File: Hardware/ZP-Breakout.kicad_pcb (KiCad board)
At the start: 4 copper layers, 100 x 75 mm, 196 parts, among them J1 GH-6, J10 GH-4, J11 GH-3, J12 GH-4, J13 GH-2, J14 GH-4, J15 GH-4, J16 GH-4, J17 GH-4, J18 GH-6, J19 GH-6, J2 GH-6, J20 GH-6, J21 GH-6, J22 GH-6, J23 GH-6, J24 GH-2, J25 GH-4, J26 GH-4, J27 GH-4, J28 GH-4, J29 GH-6, J3 GH-6, J30 Conn_02x02_Odd_Even, J31 Conn_01x02, J4 GH-6, J5 GH-6, J6 GH-6, J7 GH-2, J8 Micro_SD_Card, J9 USB_MICRO_B, Q1 BSS84LT1G, Q2 BSS138, Q3 BSS84LT1G, SW1 SW_Push_Dual_1-2short_3-4short, SW2 SW_Push_Dual_1-2short_3-4short, U1 MCP1826S-3302E/DB, U4 STM32F765ZGT6, U5 M24C64-WDW6TP, U6 ICM-20602, U7 MS5637-02BA03, U8 FT4232H, U9 STM32F091RCT7, Y1 32.768kHz, Y2 8MHz, Y3 Crystal_GND24, Y4 32.768kHz, Y5 8MHz

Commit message: Finished routing. TODO: Silk.
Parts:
- J27: value GH-4 -> GH-2; footprint Connector_PinHeader_2.54mm:PinHeader_1x04_P2.54mm_Vertical -> Connector_PinHeader_2.54mm:PinHeader_1x02_P2.54mm_Vertical
- moved J29 64.7 mm to (113.3, 93.5)
- moved J27 55.6 mm to (102.2, 98.3), turned to 270 degrees
- moved J23 32.4 mm to (104.4, 138.2)
- moved R8 20.3 mm to (59.1, 136.6)
- moved R9 20.2 mm to (60.7, 136.6), turned to 270 degrees
- moved D16 20.1 mm to (62.4, 136.7)
- moved J15 18.4 mm to (78.7, 143.2)
- moved J16 18.4 mm to (78.7, 138.2)
- moved D15 15.9 mm to (62.4, 139.9), turned to 90 degrees
- moved R7 15.1 mm to (60.7, 140.1)
- moved D2 14.7 mm to (81.2, 98.8), turned to 180 degrees
- moved Q1 13.7 mm to (84.3, 96.1), turned to 270 degrees
- moved J28 13.7 mm to (97.0, 153.1)
- moved J19 13.6 mm to (104.4, 143.1)
- moved J12 12.8 mm to (109.8, 153.2)
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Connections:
- J27 pad 1: GND -> /SCL1
- J27 pad 2: /SCL1 -> /SDA1
- J30 pad 2: /5V_INT -> /6V_EXT
- J30 pad 4: /6V_EXT -> /5V_INT
- Q1 pad 2: /5V_INT -> /3V3
- Q3 pad 2: /5V_INT -> /3V3
- R1 pad 2: /5V_INT -> /3V3
- R2 pad 2: /5V_INT -> /3V3
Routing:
- net /3V3: track 198.5 -> 248.4 mm, vias 30 -> 41
- net /NRST_SAFETY: track 31.5 -> 80.6 mm
- net /5V_INT: track 25.2 -> 72.3 mm, vias 2 -> 24
- net /NRST_PILOT: track 47.7 -> 88.1 mm, vias 7 -> 8
- net /NSS5: track 0.00 -> 36.3 mm, vias 0 -> 1
- net /AIRSPD_ADC: track 36.7 -> 72.7 mm
- net /ULTRA_SONIC_2: track 38.5 -> 73.8 mm, vias 1 -> 2
- net /CTS1: track 38.6 -> 72.1 mm, vias 4 -> 3
- net /TX2: track 6.13 -> 37.9 mm, vias 0 -> 1
- net /SDA4: track 7.46 -> 38.9 mm
- net /RX1: track 37.3 -> 68.4 mm, vias 4 -> 3
- net /RTS2: track 14.8 -> 45.1 mm
- net /TX1: track 35.1 -> 65.1 mm, vias 4 -> 3
- net /RX2: track 4.77 -> 34.0 mm, vias 0 -> 1
- net /SDA2: track 10.0 -> 38.7 mm
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- added copper zone on F.Cu, net /5V_INT
- added copper zone on F.Cu, net /5V_USB
- added copper zone on F.Cu, net /POWER/3V3_JMP
- added copper zone on PWR, net /POWER/3V3_JMP
- added copper zone on F.Cu, net /POWER/5V_INT_JMP
- added copper zone on PWR, net GND
- added copper zone on F.Cu, net Net-(C2-Pad2)
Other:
- board size 100 x 75 mm -> 100 x 65 mm
- rule trace_min: 0.0889 -> 0.2

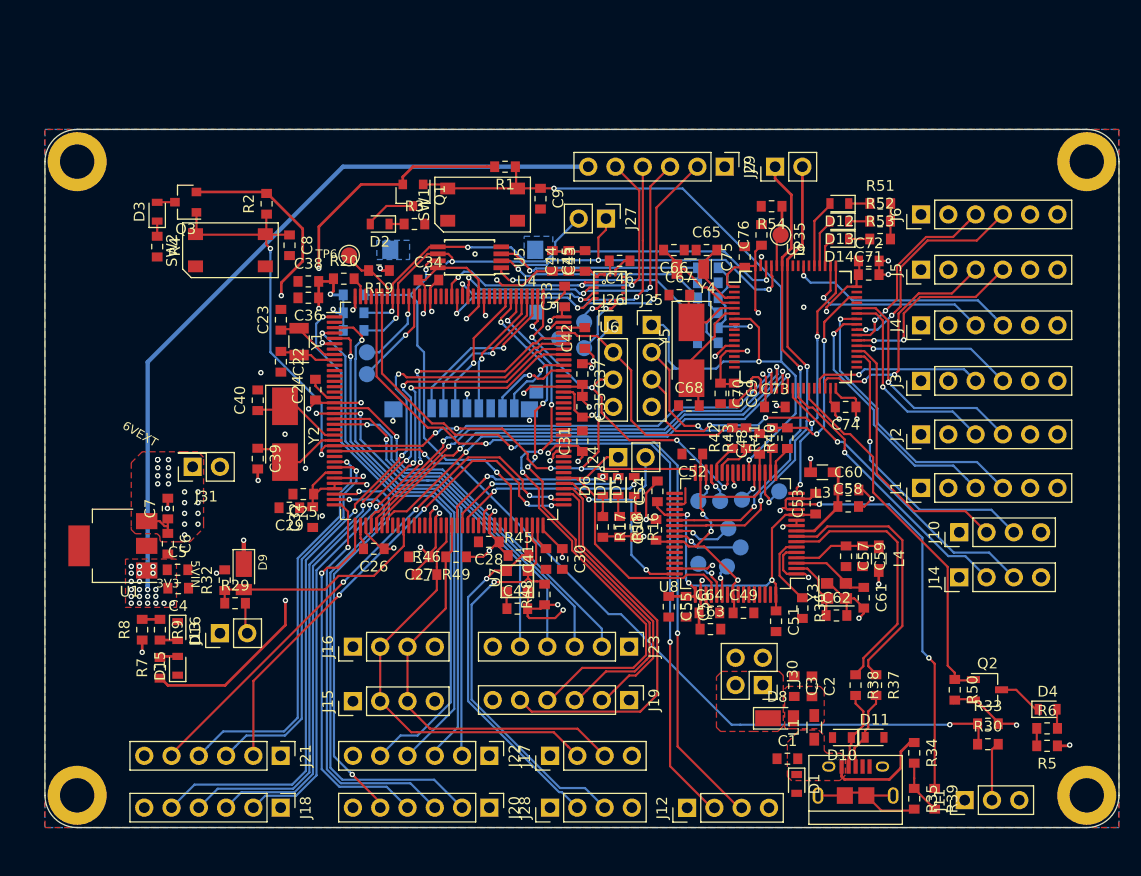
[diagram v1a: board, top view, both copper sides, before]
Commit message: Added additional headers to some interfaces, GPIOs, and FTDI pins. Added silks
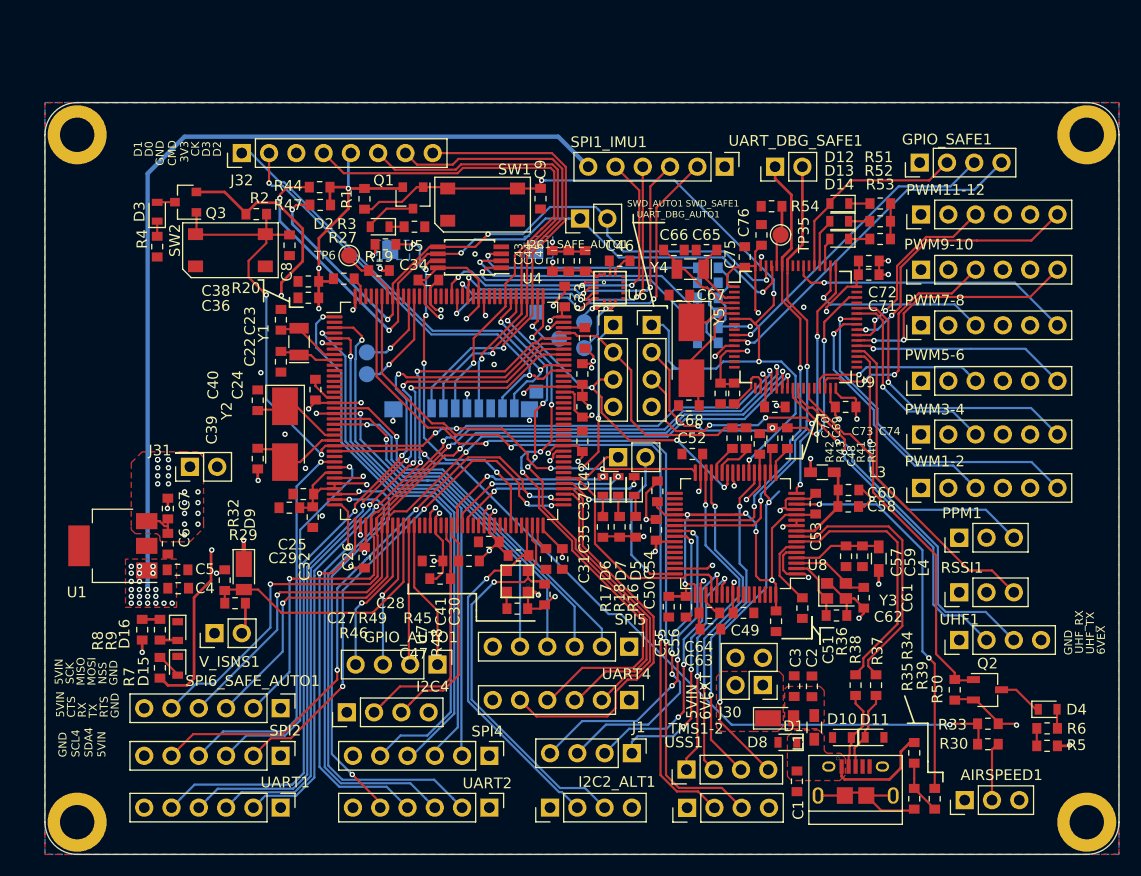
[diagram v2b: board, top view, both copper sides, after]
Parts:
- removed J12, J14, J26, J28: GH-4, Connector_PinHeader_2.54mm:PinHeader_1x04_P2.54mm_Vertical
- removed TP19: TDO1_TST, TestPoint:TestPoint_Pad_D1.5mm
- removed TP20: TMS1_TST, TestPoint:TestPoint_Pad_D1.5mm
- removed TP21: TDO2_TST, TestPoint:TestPoint_Pad_D1.5mm
- removed TP22: TMS2_TST, TestPoint:TestPoint_Pad_D1.5mm
- removed TP23: UART1_RTS_TST, TestPoint:TestPoint_Pad_D1.5mm
- removed TP24: UART1_CTS_TST, TestPoint:TestPoint_Pad_D1.5mm
- removed TP25: UART2_RTS_TST, TestPoint:TestPoint_Pad_D1.5mm
- removed TP26: UART2_CTS_TST, TestPoint:TestPoint_Pad_D1.5mm
- added I2C2_ALT1: GH-4, Connector_PinHeader_2.54mm:PinHeader_1x04_P2.54mm_Vertical, F.Cu at (97.0, 153.1)
- added J1: GH-4, Connector_PinHeader_2.54mm:PinHeader_1x04_P2.54mm_Vertical, F.Cu at (104.6, 148.1)
- added J32: CONN-8, Connector_PinHeader_2.54mm:PinHeader_1x08_P2.54mm_Vertical, F.Cu at (68.3, 92.2)
- added PPM1: GH-3, Connector_PinHeader_2.54mm:PinHeader_1x03_P2.54mm_Vertical, F.Cu at (135.1, 128.0)
- added SPI6_SAFE_AUTO1: GH-6, Connector_PinHeader_2.54mm:PinHeader_1x06_P2.54mm_Vertical, F.Cu at (71.9, 143.9)
- added SWD_AUTO1: GH-4, Connector_PinHeader_2.54mm:PinHeader_1x04_P2.54mm_Vertical, F.Cu at (102.9, 108.2)
- added TMS1-2: GH-4, Connector_PinHeader_2.54mm:PinHeader_1x04_P2.54mm_Vertical, F.Cu at (109.7, 149.6)
- added UHF1: GH-4, Connector_PinHeader_2.54mm:PinHeader_1x04_P2.54mm_Vertical, F.Cu at (135.1, 137.5)
- added USS1: GH-4, Connector_PinHeader_2.54mm:PinHeader_1x04_P2.54mm_Vertical, F.Cu at (109.8, 153.2)
- R27, R44, R47: moved to F.Cu
- RSSI1: renamed from J10; value GH-4 -> GH-3; footprint Connector_PinHeader_2.54mm:PinHeader_1x04_P2.54mm_Vertical -> Connector_PinHeader_2.54mm:PinHeader_1x03_P2.54mm_Vertical
- moved GPIO_SAFE1 69.4 mm to (131.4, 93.1)
- moved I2C4 19.4 mm to (78.1, 144.3)
- moved R44 13.7 mm to (75.6, 95.4), turned to 180 degrees
- moved R1 13.4 mm to (79.8, 96.5), turned to 90 degrees
- moved R47 10.5 mm to (75.6, 97.0), turned to 180 degrees
- moved GPIO_AUTO1 8.58 mm to (86.6, 139.8), turned to 270 degrees
- moved RSSI1 5.59 mm to (135.1, 133.1)
- moved R27 5.56 mm to (81.7, 100.7)
- moved D1 3.97 mm to (119.1, 147.1), turned to 180 degrees
- moved H1 2.50 mm to (147.0, 90.5)
- moved H2 2.50 mm to (147.0, 154.5)
- moved H3 2.50 mm to (53.0, 154.5)
- moved H4 2.50 mm to (53.0, 90.5)
- moved I2C1_SAFE_AUTO1 2.41 mm to (99.8, 98.3), turned to 90 degrees
- moved C1 2.28 mm to (120.0, 150.7), turned to 90 degrees
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- renumbered J11 to AIRSPEED1, J15 to GPIO_AUTO1, J16 to GPIO_SAFE1, J27 to I2C1_SAFE_AUTO1, J17 to I2C4, J1 to PWM1-2, J6 to PWM11-12, J2 to PWM3-4, J3 to PWM5-6, J4 to PWM7-8, J5 to PWM9-10, J29 to SPI1_IMU1, J21 to SPI2, J22 to SPI4, J23 to SPI5, J25 to SWD_SAFE1, J18 to UART1, J20 to UART2, J19 to UART4, J24 to UART_DBG_AUTO1, J7 to UART_DBG_SAFE1, J13 to V_ISNS1
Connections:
- D12 pad 2: Net-(D12-Pad2) -> /S_PC12
- GPIO_AUTO1 pad 1: GND -> /PB2
- GPIO_AUTO1 pad 2: /SCL4 -> /PB1
- GPIO_AUTO1 pad 3: /SDA4 -> /PC5
- GPIO_AUTO1 pad 4: /5V_INT -> /PC4
- GPIO_SAFE1 pad 2: /SCL4 -> /S_PC12
- GPIO_SAFE1 pad 3: /SDA4 -> /S_PC2
- GPIO_SAFE1 pad 4: /5V_INT -> /S_PC3
- PWM1-2 pad 2: GND -> /6V_EXT
- PWM1-2 pad 4: /PWM 1-12/PWM2 -> GND
- PWM1-2 pad 6: /6V_EXT -> /PWM 1-12/PWM2
- PWM11-12 pad 2: GND -> /6V_EXT
- PWM11-12 pad 4: /PWM 1-12/PWM12 -> GND
- PWM11-12 pad 6: /6V_EXT -> /PWM 1-12/PWM12
- PWM3-4 pad 2: GND -> /6V_EXT
- PWM3-4 pad 4: /PWM 1-12/PWM4 -> GND
- PWM3-4 pad 6: /6V_EXT -> /PWM 1-12/PWM4
- PWM5-6 pad 2: GND -> /6V_EXT
- PWM5-6 pad 4: /PWM 1-12/PWM6 -> GND
- PWM5-6 pad 6: /6V_EXT -> /PWM 1-12/PWM6
- PWM7-8 pad 2: GND -> /6V_EXT
- PWM7-8 pad 4: /PWM 1-12/PWM8 -> GND
- PWM7-8 pad 6: /6V_EXT -> /PWM 1-12/PWM8
- PWM9-10 pad 2: GND -> /6V_EXT
- PWM9-10 pad 4: /PWM 1-12/PWM10 -> GND
- PWM9-10 pad 6: /6V_EXT -> /PWM 1-12/PWM10
- RSSI1 pad 2: /RSSI -> Net-(RSSI1-Pad2)
- RSSI1 pad 3: /PPM -> /RSSI
- U4 pad 44: Net-(U4-Pad44) -> /PC4
- U4 pad 45: Net-(U4-Pad45) -> /PC5
- U4 pad 47: Net-(U4-Pad47) -> /PB1
- U4 pad 48: Net-(U4-Pad48) -> /PB2
- U9 pad 10: Net-(U9-Pad10) -> /S_PC2
- U9 pad 11: Net-(U9-Pad11) -> /S_PC3
- U9 pad 53: Net-(D12-Pad2) -> /S_PC12
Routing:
- net /SD_D1: track 7.29 -> 43.5 mm
- net /SD_CMD: track 12.4 -> 48.5 mm
- net /SD_D0: track 8.05 -> 43.0 mm, vias 1 -> 2
- net /S_PC3: track 0.00 -> 31.9 mm, vias 0 -> 1
- net /3V3: track 248.4 -> 216.6 mm, vias 41 -> 42
- net /SCK6: track 46.5 -> 77.9 mm, vias 2 -> 3
- net /SD_CK: track 12.1 -> 43.1 mm
- net /S_PC2: track 0.00 -> 29.0 mm, vias 0 -> 1
- net /SD_D3: track 14.8 -> 43.7 mm
- net /MISO6: track 45.4 -> 74.2 mm, vias 2 -> 3
- net /TDO1_TST: track 4.37 -> 33.0 mm, vias 1 -> 2
- net /TMS1_TST: track 3.02 -> 31.0 mm, vias 1 -> 2
- net /TMS2_TST: track 3.04 -> 31.0 mm, vias 1 -> 2
- net /TDO2_TST: track 3.00 -> 30.7 mm, vias 1 -> 2
- net /MOSI6: track 44.6 -> 72.1 mm, vias 2 -> 3
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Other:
- board size 100 x 65 mm -> 100 x 70 mm
- board text added: "6VEX"
- board text added: "CK"
- board text added: "CMD"
- board text added: "CTS"
- board text added: "D0"
- board text added: "D1"
- board text added: "D2"
- board text added: "D3"
- board text added: "GND"
- board text added: "GND SCL4 SDA4 5VIN"
- board text added: "GND USS1 USS2 5VIN"
- board text added: "IMU_FSYNC"
- board text added: "IMU_INT"
- board text added: "MISO"
- board text added: "MOSI"
- board text added: "NSS"
- board text added: "RTS"
- board text added: "RX"
- board text added: "SCK"
- board text added: "TDI"
- board text added: "TMS2 TDO2 TMS1 TDO1"
- board text added: "TX"
- board text added: "UHF_RX"
- board text added: "UHF_TX"
- board text added: "WARG ZP-Breakout"
- board text removed: "5V CTS RX TX RTS GND"
- board text removed: "5V SCK MISO MOSI NSS GND"
- board text removed: "5V SDA SCL GND"
- board text removed: "GND SCL SDA 5V"
- board text removed: "WARG ZeroPilot"
